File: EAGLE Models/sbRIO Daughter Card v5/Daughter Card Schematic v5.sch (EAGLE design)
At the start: 68 parts, among them IC1 BTS716G, IC2 BTS716G, IC3 BTS716G, Q7 MMBT4403-7-F, Q8 MMBT4403-7-F, U2 ADXL345, U3 L3G4200D, X1 5566-2

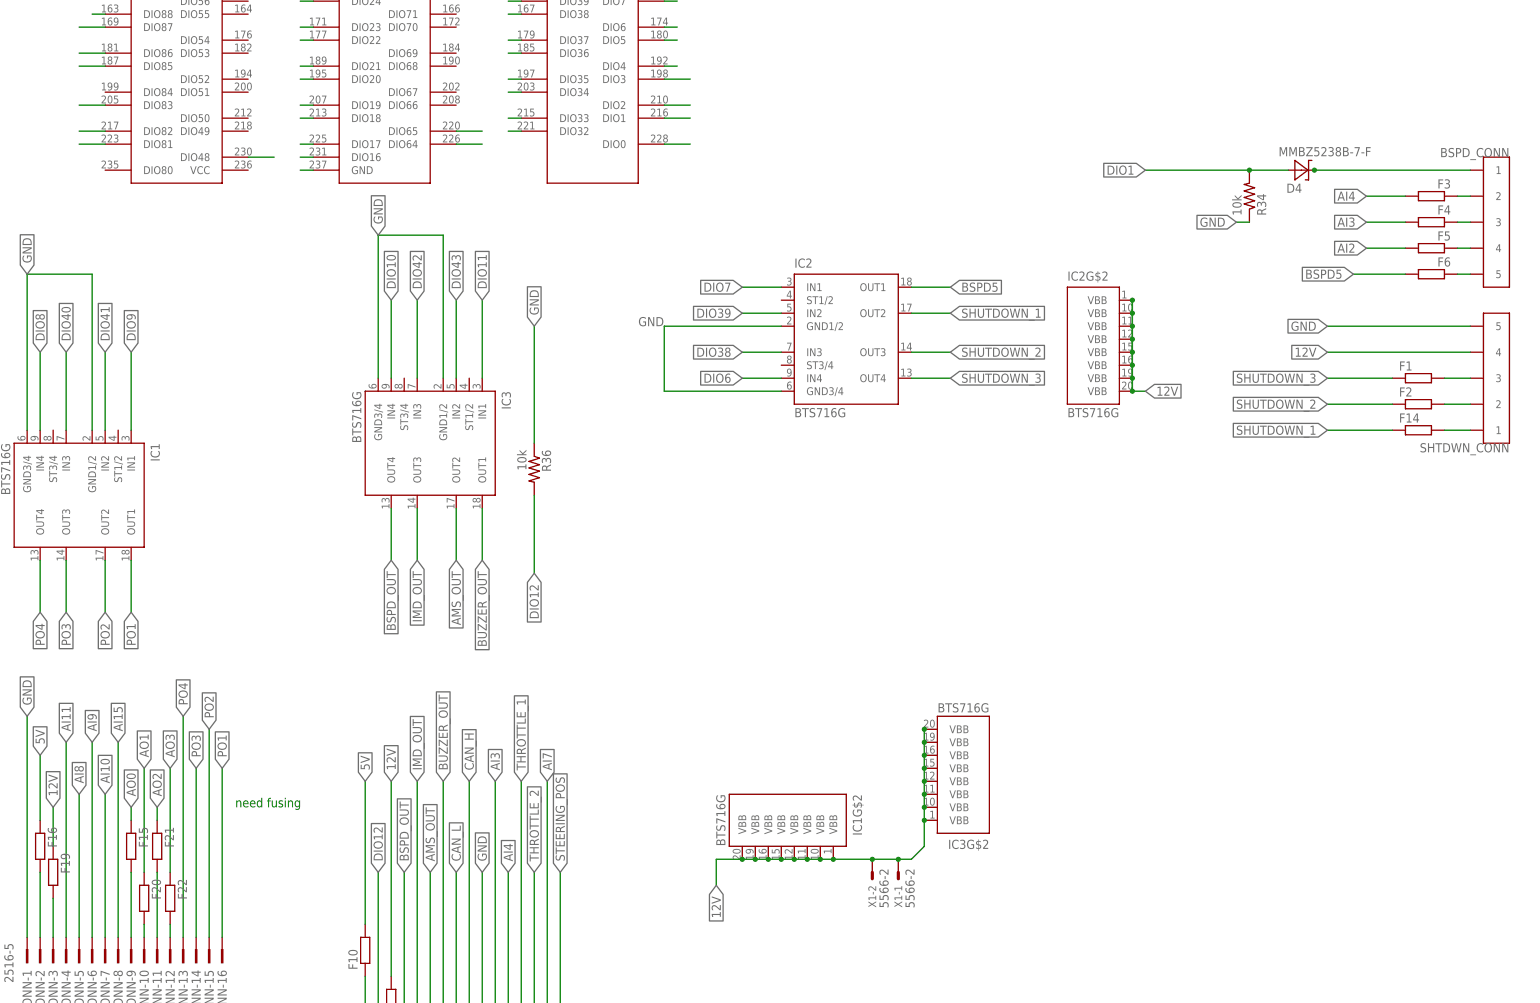
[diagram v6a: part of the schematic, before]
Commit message: Made layout pass DRC
also added level shifted inputs for wheel speeds
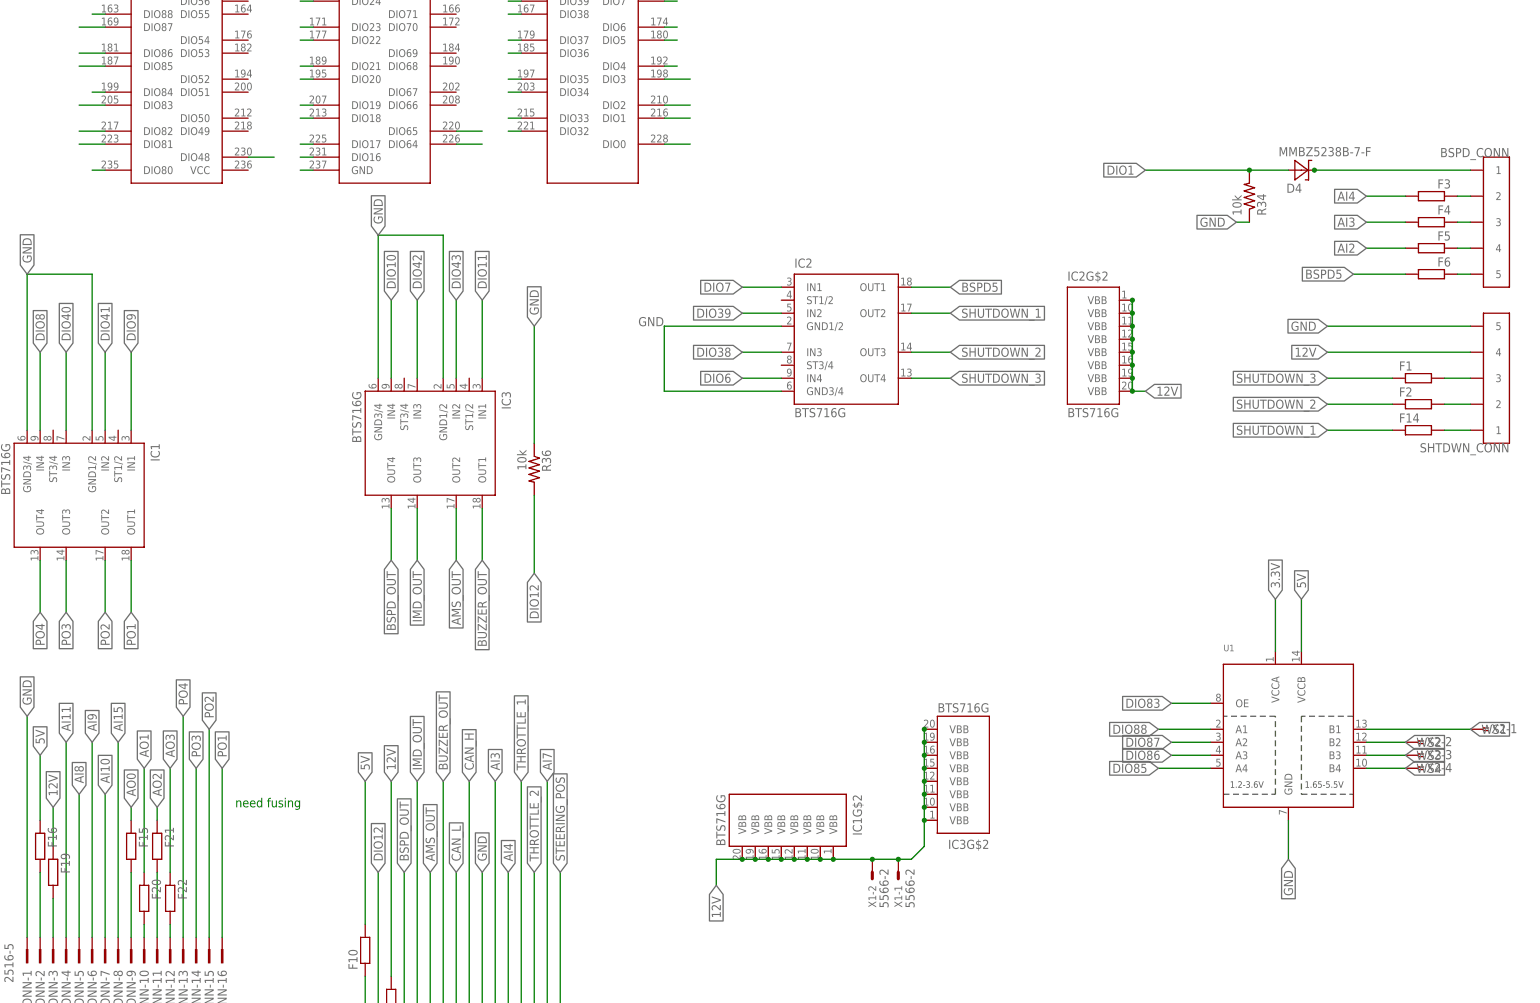
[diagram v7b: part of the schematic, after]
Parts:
- added U1: (no value), SparkFun-DigitalIC:TXB0104PWR
- added X2: (no value), con-amp:FTOP-4
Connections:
- removed net N$24: U$3.DIO88
- new net DIO80: U$3.DIO80
- new net DIO84: U$3.DIO84
- new net DIO88: U$3.DIO88, U1.A1
- new net WS1: U1.B1, X2-1.1
- new net WS2: U1.B2, X2-2.1
- new net WS3: U1.B3, X2-3.1
- new net WS4: U1.B4, X2-4.1
- net 3.3V: now also U1.VCCA
- net 5V: now also U1.VCCB
- net DIO83: now also U1.OE
- net DIO85: now also U1.A4
- net DIO86: now also U1.A3
- net DIO87: now also U1.A2
- net GND: now also U1.GND
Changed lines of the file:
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@@
 <part name="F10" library="resistor" deviceset="R-EU_" device="R0402"/>
 <part name="X1" library="con-molex" deviceset="5566-2" device=""/>
+<part name="U1" library="SparkFun-DigitalIC" deviceset="TXB0104PWR" device=""/>
+<part name="X2" library="con-amp" deviceset="FTOP-4" device=""/>
 </parts>
 <sheets>
@@
 <instance part="X1" gate="-1" x="299.72" y="-167.64" rot="R270"/>
 <instance part="X1" gate="-2" x="294.64" y="-167.64" rot="R270"/>
+<instance part="U1" gate="G$1" x="375.92" y="-142.24"/>
+<instance part="X2" gate="-1" x="414.02" y="-139.7"/>
+<instance part="X2" gate="-2" x="401.32" y="-142.24"/>
+<instance part="X2" gate="-3" x="401.32" y="-144.78"/>
+<instance part="X2" gate="-4" x="401.32" y="-147.32"/>
 </instances>
 <busses>
@@
 <label x="248.92" y="-60.96" size="1.778" layer="95"/>
 </segment>
+<segment>
+<pinref part="U1" gate="G$1" pin="GND"/>
+<wire x1="375.92" y1="-157.48" x2="375.92" y2="-165.1" width="0.1524" layer="91"/>
+<label x="375.92" y="-165.1" size="1.778" layer="95" rot="R270" xref="yes"/>
+</segment>
 </net>
 <net name="12V" class="0">
@@
 <label x="-111.76" y="27.94" size="1.778" layer="95" rot="R90" xref="yes"/>
 </segment>
+<segment>
+<pinref part="U1" gate="G$1" pin="VCCB"/>
+<wire x1="378.46" y1="-124.46" x2="378.46" y2="-114.3" width="0.1524" layer="91"/>
+<label x="378.46" y="-114.3" size="1.778" layer="95" rot="R90" xref="yes"/>
+</segment>
 </net>
 <net name="DIO3" class="0">
@@
 <junction x="261.62" y="111.76"/>
 </segment>
+<segment>
+<pinref part="U1" gate="G$1" pin="VCCA"/>
+<wire x1="373.38" y1="-124.46" x2="373.38" y2="-114.3" width="0.1524" layer="91"/>
+<label x="373.38" y="-114.3" size="1.778" layer="95" rot="R90" xref="yes"/>
+</segment>
 </net>
 <net name="DIO29" class="0">
@@
 <wire x1="144.78" y1="-17.78" x2="139.7" y2="-17.78" width="0.1524" layer="91"/>
 </segment>
+<segment>
+<pinref part="U1" gate="G$1" pin="OE"/>
+<wire x1="360.68" y1="-134.62" x2="353.06" y2="-134.62" width="0.1524" layer="91"/>
+<label x="353.06" y="-134.62" size="1.778" layer="95" rot="R180" xref="yes"/>
+</segment>
 </net>
 <net name="DIO85" class="0">
@@
 <wire x1="144.78" y1="-10.16" x2="139.7" y2="-10.16" width="0.1524" layer="91"/>
 </segment>
+<segment>
+<pinref part="U1" gate="G$1" pin="A4"/>
+<wire x1="360.68" y1="-147.32" x2="350.52" y2="-147.32" width="0.1524" layer="91"/>
+<label x="350.52" y="-147.32" size="1.778" layer="95" rot="R180" xref="yes"/>
+</segment>
 </net>
 <net name="DIO86" class="0">
@@
 <wire x1="144.78" y1="-7.62" x2="139.7" y2="-7.62" width="0.1524" layer="91"/>
 </segment>
+<segment>
+<pinref part="U1" gate="G$1" pin="A3"/>
+<wire x1="360.68" y1="-144.78" x2="353.06" y2="-144.78" width="0.1524" layer="91"/>
+<label x="353.06" y="-144.78" size="1.778" layer="95" rot="R180" xref="yes"/>
+</segment>
 </net>
 <net name="DIO87" class="0">
@@
 <wire x1="144.78" y1="-2.54" x2="139.7" y2="-2.54" width="0.1524" layer="91"/>
 </segment>
-</net>
-<net name="N$24" class="0">
+<segment>
+<pinref part="U1" gate="G$1" pin="A2"/>
+<wire x1="360.68" y1="-142.24" x2="353.06" y2="-142.24" width="0.1524" layer="91"/>
+<label x="353.06" y="-142.24" size="1.778" layer="95" rot="R180" xref="yes"/>
+</segment>
+</net>
+<net name="DIO88" class="0">
 <segment>
 <pinref part="U$3" gate="G$1" pin="DIO88"/>
 <wire x1="144.78" y1="0" x2="142.24" y2="0" width="0.1524" layer="91"/>
+</segment>
+<segment>
+<pinref part="U1" gate="G$1" pin="A1"/>
+<wire x1="360.68" y1="-139.7" x2="350.52" y2="-139.7" width="0.1524" layer="91"/>
+<label x="350.52" y="-139.7" size="1.778" layer="95" rot="R180" xref="yes"/>
 </segment>
 </net>
@@
 </segment>
 </net>
+<net name="WS1" class="0">
+<segment>
+<pinref part="U1" gate="G$1" pin="B1"/>
+<wire x1="391.16" y1="-139.7" x2="411.48" y2="-139.7" width="0.1524" layer="91"/>
+<label x="411.48" y="-139.7" size="1.778" layer="95" xref="yes"/>
+<pinref part="X2" gate="-1" pin="1"/>
+</segment>
+</net>
+<net name="WS2" class="0">
+<segment>
+<pinref part="U1" gate="G$1" pin="B2"/>
+<wire x1="391.16" y1="-142.24" x2="398.78" y2="-142.24" width="0.1524" layer="91"/>
+<label x="398.78" y="-142.24" size="1.778" layer="95" xref="yes"/>
+<pinref part="X2" gate="-2" pin="1"/>
+</segment>
+</net>
+<net name="WS3" class="0">
+<segment>
+<pinref part="U1" gate="G$1" pin="B3"/>
+<wire x1="391.16" y1="-144.78" x2="398.78" y2="-144.78" width="0.1524" layer="91"/>
+<label x="398.78" y="-144.78" size="1.778" layer="95" xref="yes"/>
+<pinref part="X2" gate="-3" pin="1"/>
+</segment>
+</net>
+<net name="WS4" class="0">
+<segment>
+<pinref part="U1" gate="G$1" pin="B4"/>
+<wire x1="391.16" y1="-147.32" x2="398.78" y2="-147.32" width="0.1524" layer="91"/>
+<label x="398.78" y="-147.32" size="1.778" layer="95" xref="yes"/>
+<pinref part="X2" gate="-4" pin="1"/>
+</segment>
+</net>
+<net name="DIO84" class="0">
+<segment>
+<pinref part="U$3" gate="G$1" pin="DIO84"/>
+<wire x1="144.78" y1="-15.24" x2="142.24" y2="-15.24" width="0.1524" layer="91"/>
+</segment>
+</net>
+<net name="DIO80" class="0">
+<segment>
+<pinref part="U$3" gate="G$1" pin="DIO80"/>
+<wire x1="144.78" y1="-30.48" x2="142.24" y2="-30.48" width="0.1524" layer="91"/>
+</segment>
+</net>
